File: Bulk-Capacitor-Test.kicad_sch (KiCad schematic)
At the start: 62 parts, among them J1 Conn_01x01_Socket, J2 Conn_01x01_Socket, J3 Conn_01x01_Socket, J4 Conn_01x01_Socket

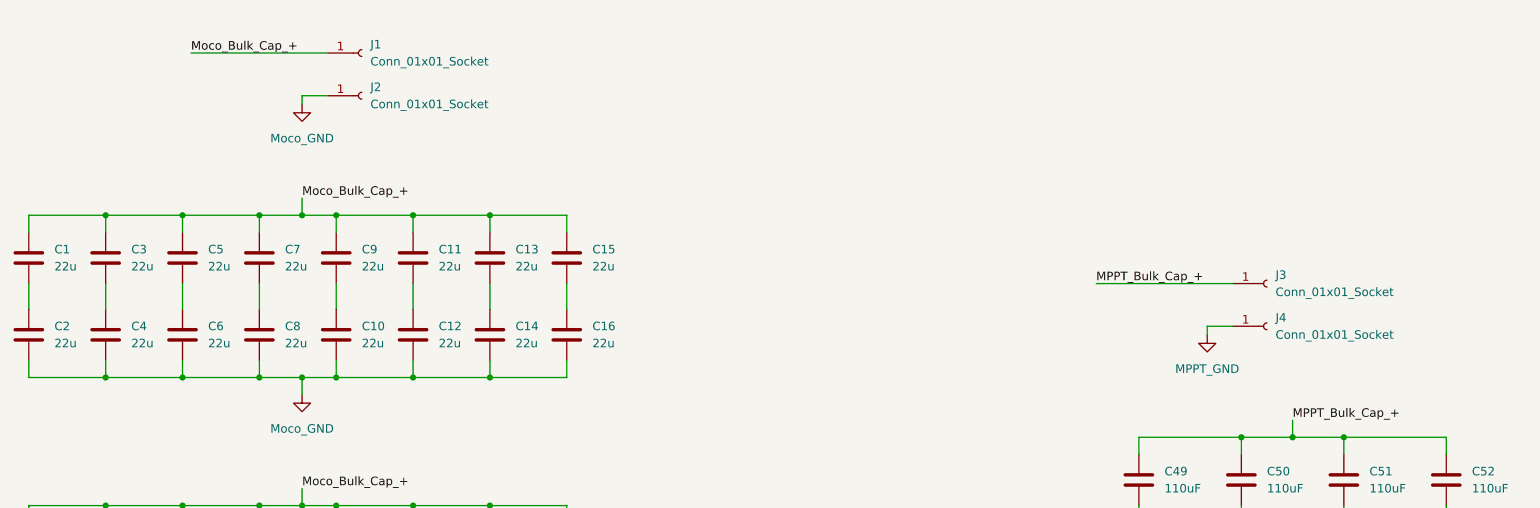
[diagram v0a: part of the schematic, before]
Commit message: added testpoints
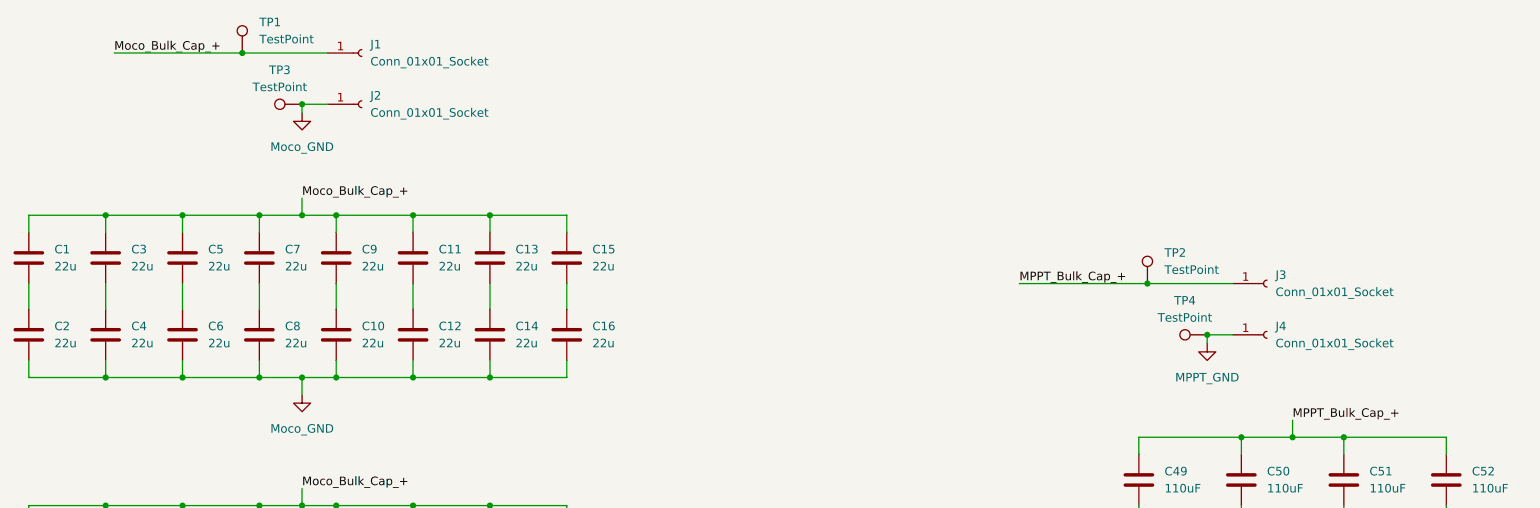
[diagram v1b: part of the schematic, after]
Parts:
- added TP1, TP2, TP3, TP4: TestPoint, BCT:5281, symbol Connector:TestPoint
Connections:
- net MPPT_Bulk_Cap_+: now also TP2.1
- net MPPT_GND: now also TP4.1
- net Moco_Bulk_Cap_+: now also TP1.1
- net Moco_GND: now also TP3.1
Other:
- moved on the sheet: J2, J4

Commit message: now two boards
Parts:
- added H7, H8: MountingHole, MountingHole:MountingHole_3mm, symbol Mechanical:MountingHole
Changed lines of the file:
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@@
+	)
+	(symbol
+		(lib_id "Mechanical:MountingHole")
+		(at 157.48 156.21 0)
+		(unit 1)
+		(exclude_from_sim yes)
+		(in_bom no)
+		(on_board yes)
+		(dnp no)
+		(fields_autoplaced yes)
+		(property "Reference" "H8"
+			(at 160.02 154.9399 0)
+			(effects
+				(font
+					(size 1.27 1.27)
+				)
+				(justify left)
+			)
+		)
+		(property "Value" "MountingHole"
+			(at 160.02 157.4799 0)
+			(effects
+				(font
+					(size 1.27 1.27)
+				)
+				(justify left)
+			)
+		)
+		(property "Footprint" "MountingHole:MountingHole_3mm"
+			(at 157.48 156.21 0)
+			(effects
+				(font
+					(size 1.27 1.27)
+				)
+				(hide yes)
+			)
+		)
+		(property "Datasheet" "~"
+			(at 157.48 156.21 0)
+			(effects
+				(font
+					(size 1.27 1.27)
+				)
+				(hide yes)
+			)
+		)
+		(property "Description" "Mounting Hole without connection"
+			(at 157.48 156.21 0)
+			(effects
+				(font
+					(size 1.27 1.27)
+				)
+				(hide yes)
+			)
+		)
+		(instances
+			(project "Bulk-Capacitor-Test"
+				(path "/35efaa0f-d287-4350-a8e0-cf10c10ae97b"
+					(reference "H8")
+					(unit 1)
+				)
+			)
+		)
 	)
 	(symbol
@@
 					(unit 1)
 				)
+			)
+		)
+	)
+	(symbol
+		(lib_id "Mechanical:MountingHole")
+		(at 157.48 151.13 0)
+		(unit 1)
+		(exclude_from_sim yes)
+		(in_bom no)
+		(on_board yes)
+		(dnp no)
+		(fields_autoplaced yes)
+		(property "Reference" "H7"
+			(at 160.02 149.8599 0)
+			(effects
+				(font
+					(size 1.27 1.27)
+				)
+				(justify left)
+			)
+		)
+		(property "Value" "MountingHole"
+			(at 160.02 152.3999 0)
+			(effects
+				(font
+					(size 1.27 1.27)
+				)
+				(justify left)
+			)
+		)
+		(property "Footprint" "MountingHole:MountingHole_3mm"
+			(at 157.48 151.13 0)
+			(effects
+				(font
+					(size 1.27 1.27)
+				)
+				(hide yes)
+			)
+		)
+		(property "Datasheet" "~"
+			(at 157.48 151.13 0)
+			(effects
+				(font
+					(size 1.27 1.27)
+				)
+				(hide yes)
+			)
+		)
+		(property "Description" "Mounting Hole without connection"
+			(at 157.48 151.13 0)
+			(effects
+				(font
+					(size 1.27 1.27)
+				)
+				(hide yes)
+			)
+		)
+		(instances
+			(project "Bulk-Capacitor-Test"
+				(path "/35efaa0f-d287-4350-a8e0-cf10c10ae97b"
+					(reference "H7")
+					(unit 1)
+				)
